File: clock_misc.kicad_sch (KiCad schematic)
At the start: 12 parts, among them Y1 Osc60MHz

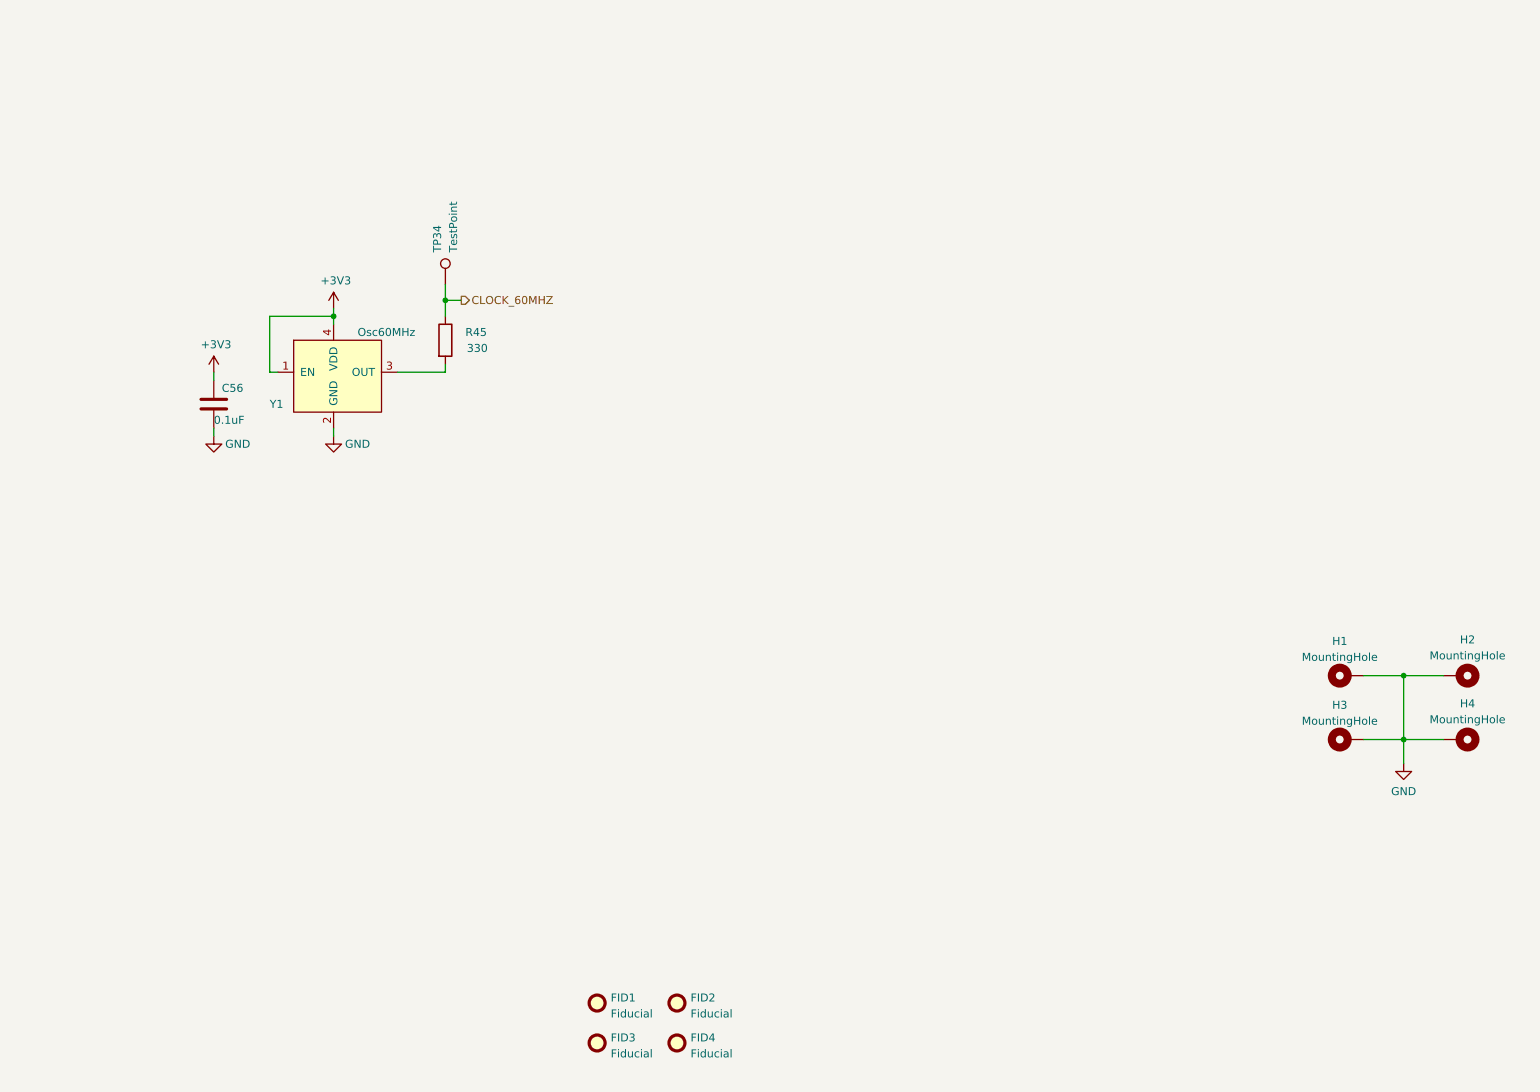
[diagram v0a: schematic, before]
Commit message: Add radio transceiver
Remove Cynthion-specific features
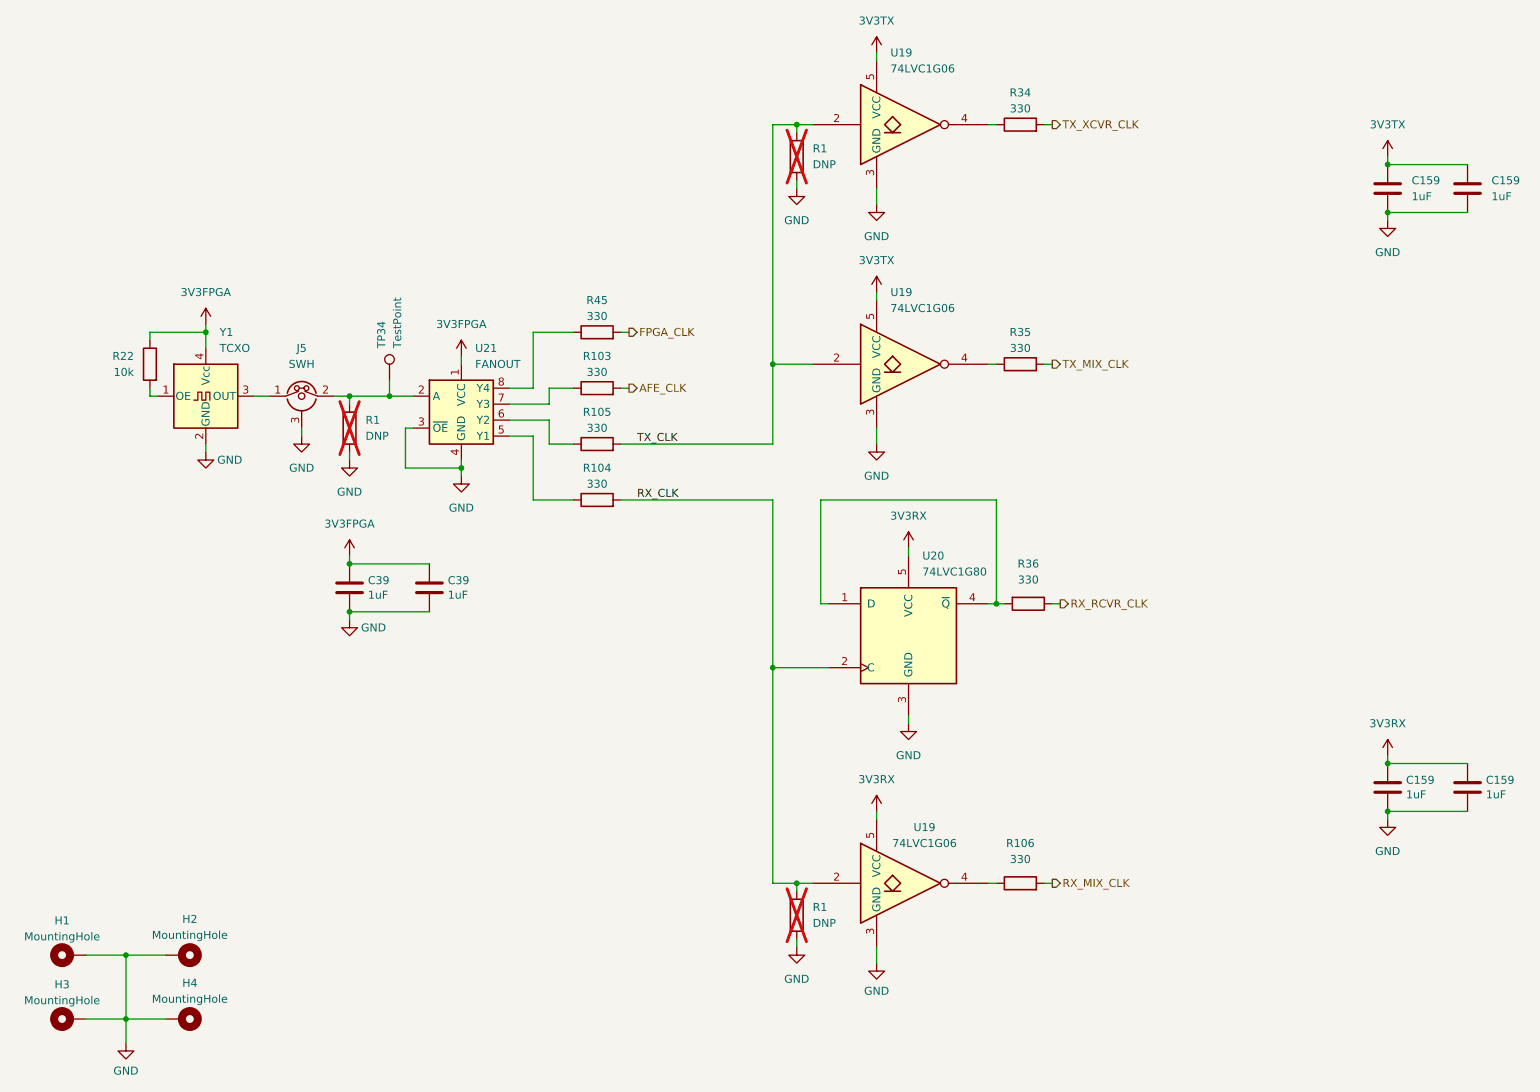
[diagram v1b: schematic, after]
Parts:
- removed C56: 0.1uF, Capacitor_SMD:C_0402_1005Metric, symbol Device:C
- removed FID1, FID2, FID3, FID4: Fiducial, Fiducial:Fiducial_0.5mm_Mask1mm, symbol Mechanical:Fiducial
- removed Y1: Osc60MHz, Crystal:Crystal_SMD_3225-4Pin_3.2x2.5mm, symbol support_hardware:DSC60xx
- added C159 (x4), C39 (x2): 1uF, Capacitor_SMD:C_0402_1005Metric, symbol Device:C
- added J5: SWH, mainboard:Murata_SWH_MM8930-26xx, symbol radio:Conn_Coaxial_MM8930-2620
- added R1 (x3): DNP, Resistor_SMD:R_0402_1005Metric, symbol Device:R
- added R103, R104, R105, R106, R34, R35, R36: 330, Resistor_SMD:R_0402_1005Metric, symbol Device:R
- added R22: 10k, Resistor_SMD:R_0402_1005Metric, symbol Device:R
- added U19 (x3): 74LVC1G06, Package_TO_SOT_SMD:SOT-353_SC-70-5, symbol 74xGxx:74LVC1G06
- added U20: 74LVC1G80, Package_TO_SOT_SMD:SOT-353_SC-70-5, symbol 74xGxx:74AUP1G80
- added U21: FANOUT, mainboard:Nexperia_XSON-8_1.95x1mm_P0.5mm, symbol support_hardware:74AVC9112
- added Y1: TCXO, Oscillator:Oscillator_SMD_Kyocera_KC2520Z-4Pin_2.5x2.0mm, symbol Oscillator:SG-210SCD
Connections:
- net GND: now also C159.2, C159.2, C159.2, C159.2, C39.2, C39.2, J5.3 (Ext), R1.2, R1.2, R1.2, U19.3 (GND), U19.3 (GND), U19.3 (GND), U20.3 (GND), U21.3 (~{OE}), U21.4 (GND), Y1.2 (GND)
- net FPGA_CLK: now reaches R45.2
- net CLOCK_60MHZ: no longer names the net of TP34.1
- net CLOCK_60MHZ: now also J5.2 (R), R1.1, U21.2 (A); no longer R45.1
- new net: R105.1, U21.6 (Y2)
- new net: R104.1, U21.5 (Y1)
- new net: R103.1, U21.7 (Y3)
- new net: R45.1, U21.8 (Y4)
- new net: R35.1, U19.4
- new net: R36.2, U20.1 (D), U20.4 (~{Q})
- new net: R22.2, Y1.1 (OE)
- new net: R34.1, U19.4
- new net: J5.1 (C), Y1.3 (OUT)
- new net: R106.1, U19.4
- new net 3V3FPGA: C39.1, C39.1, R22.1, U21.1 (VCC), Y1.4 (Vcc)
- new net 3V3RX: C159.1, C159.1, U19.5 (VCC), U20.5 (VCC)
- new net 3V3TX: C159.1, C159.1, U19.5 (VCC), U19.5 (VCC)
- new net AFE_CLK: R103.2
- new net RX_CLK: R1.1, R104.2, U19.2, U20.2 (C)
- new net RX_MIX_CLK: R106.2
- new net RX_RCVR_CLK: R36.1
- new net TX_CLK: R1.1, R105.2, U19.2, U19.2
- new net TX_MIX_CLK: R35.2
- new net TX_XCVR_CLK: R34.2
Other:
- company: Copyright 2023 Great Scott Gadgets -> ${COPYRIGHT}
- title: URTI Mainboard -> ${TITLE}
- moved on the sheet: H1, H2, H3, H4, R45, TP34

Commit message: Replace open drain clock inverters with push-pull
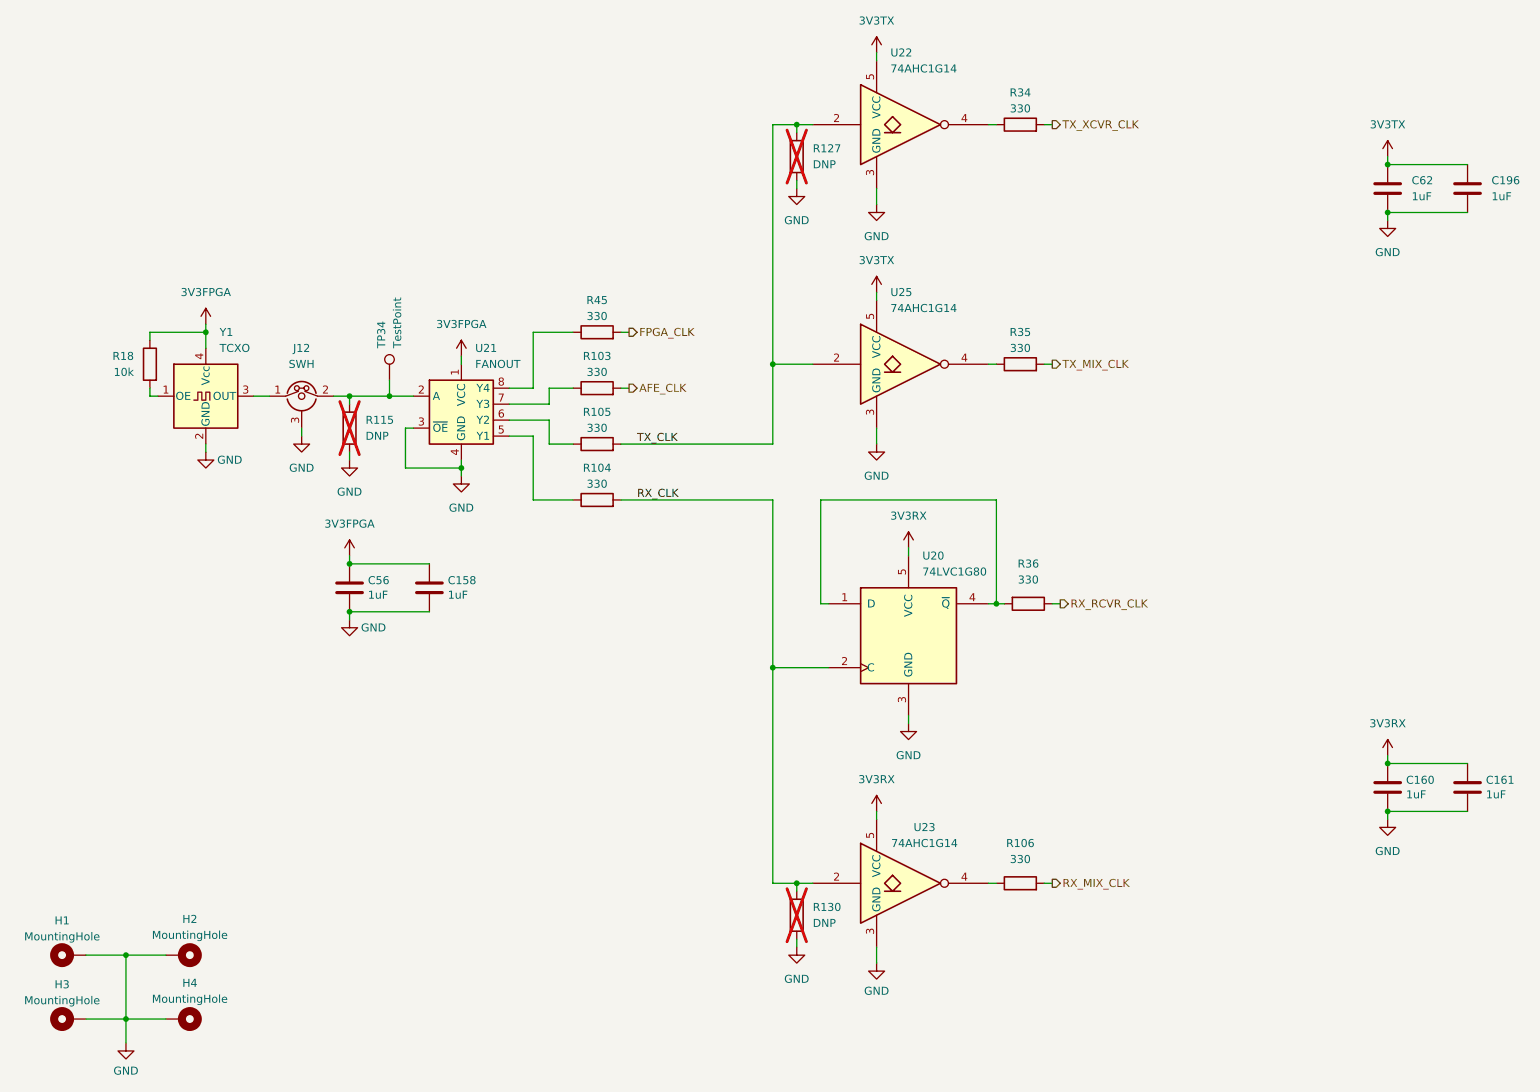
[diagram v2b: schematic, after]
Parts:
- U22: renamed from U19; value 74LVC1G06 -> 74AHC1G14; Manufacturer Nexperia -> Diodes Inc.; Part Number 74LVC1G06GW,125 -> 74AHC1G14SE-7
- U23, U25: renamed from U19; value 74LVC1G06 -> 74AHC1G14; Manufacturer Nexperia -> Diodes Inc.; Part Number 74LVC1G06GW,125 -> 74AHC1G14SE-7; Substitution (none) -> 74AHC1G14
- renumbered C39 to C158, C159 to C160, C159 to C161, C159 to C196, C39 to C56, C159 to C62, J5 to J12, R1 to R115, R1 to R127, R1 to R130, R22 to R18
